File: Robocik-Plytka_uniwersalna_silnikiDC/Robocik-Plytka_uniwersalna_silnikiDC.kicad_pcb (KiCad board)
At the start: 2 copper layers, 60 x 71.1 mm, 67 parts, among them IC1 ACSL-6400-00TE, IC2 L6205D, J1 Conn_01x03, J2 Conn_01x02, J3 Conn_01x04, J4 Conn_01x02, J5 Conn_01x03, J6 Conn_01x02, Q1 BC847, Q2 BC847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

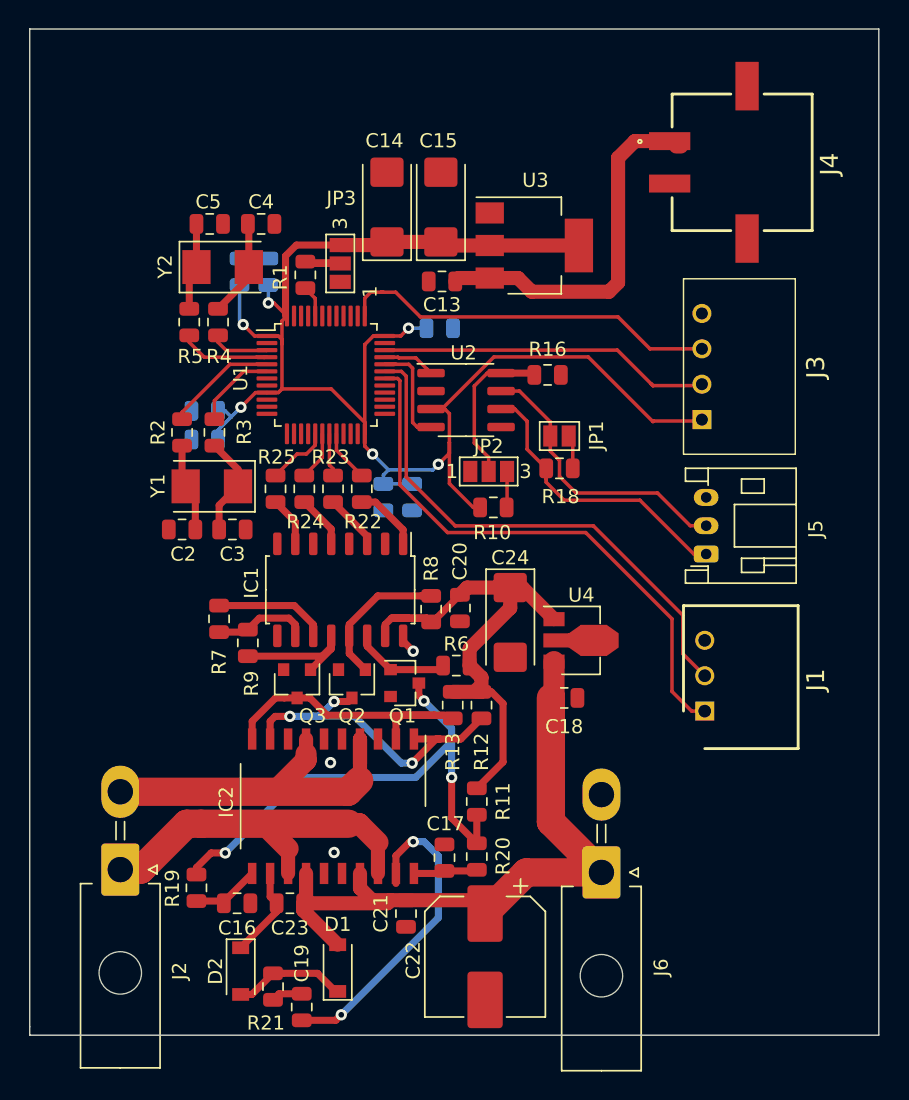
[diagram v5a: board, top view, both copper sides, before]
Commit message: Added 3D model to all connectors, fixed some connections on PCB. Added ground layers for both GNDA and GNDD.
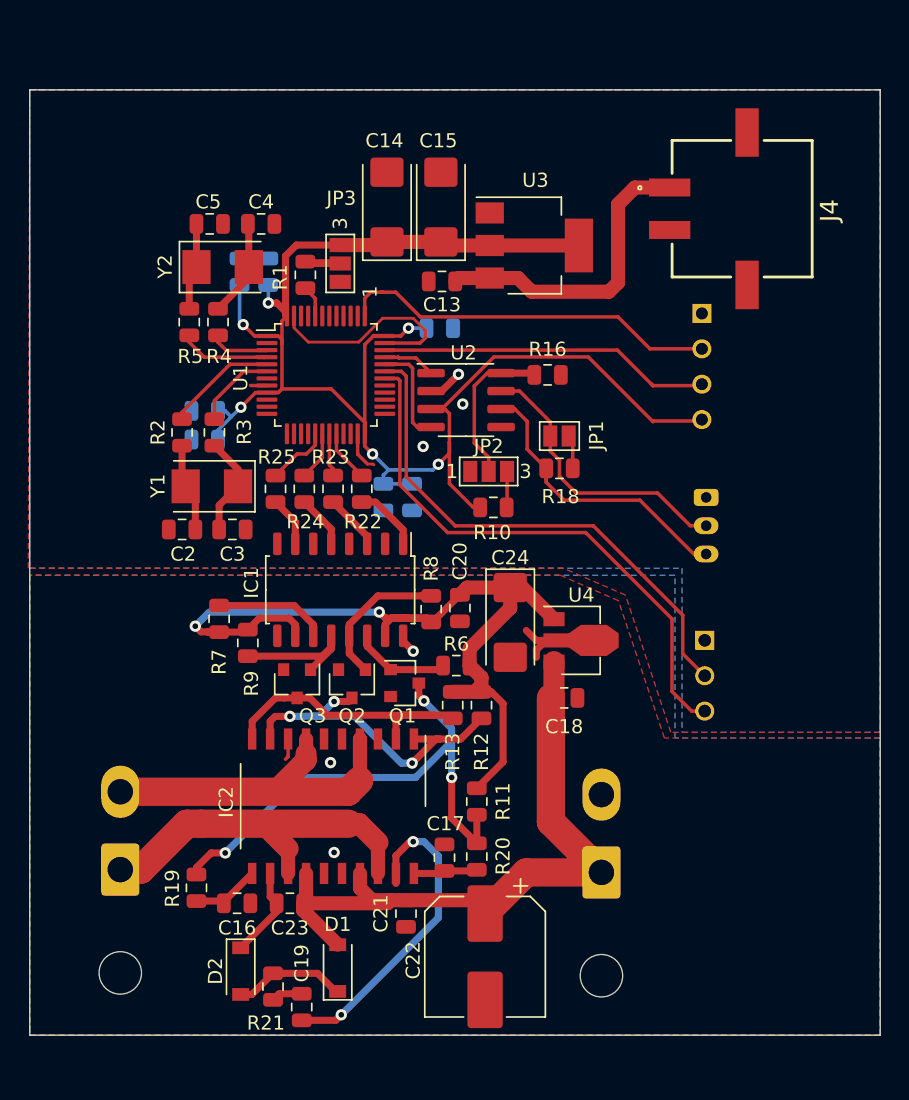
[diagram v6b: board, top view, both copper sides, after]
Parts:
- J1, J2, J3, J5, J6: moved to B.Cu
- moved J3 7.50 mm to (169.5, 85.1), turned to 90 degrees
- moved J1 5.00 mm to (169.7, 108.2), turned to 90 degrees
- moved J5 4.00 mm to (169.8, 98.1), turned to 270 degrees
- moved J4 3.28 mm to (177.3, 77.7)
- turned J2 to 0 degrees
- turned J6 to 0 degrees
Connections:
- J1 pad 1: USART_RX -> GNDD
- J1 pad 3: GNDD -> USART_RX
- J3 pad 1: 3.3VD -> GNDD
- J3 pad 2: JTMS_SWDIO -> JTCK_SWCLK
- J3 pad 3: JTCK_SWCLK -> JTMS_SWDIO
- J3 pad 4: GNDD -> 3.3VD
- J5 pad 1: CAN_L -> GNDD
- J5 pad 3: GNDD -> CAN_L
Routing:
- net GNDD: track 0.00 -> 21.7 mm, vias 0 -> 3
- net 5VPWR: track 48.6 -> 65.0 mm, vias 0 -> 2
- net GNDA: track 1.38 -> 7.47 mm
- net VddD: track 27.2 -> 21.9 mm
- added copper zone on B.Cu, net GNDA
- added copper zone on F.Cu, net GNDA
- added copper zone on B.Cu, net GNDD
- added copper zone on F.Cu, net GNDD
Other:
- board size 60 x 71.1 mm -> 60.1 x 66.8 mm

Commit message: Moved all connectors to the same side of PCB. Redesigned ground planes. Added folder "quick view" which consists of PCB schematic, layout, jpegs of PCB top and bottom side and new added step 3D model.
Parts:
- J1, J2, J3, J5, J6: moved to F.Cu
- moved J3 10.5 mm to (169.5, 95.6), turned to 270 degrees
- moved J1 8.00 mm to (169.7, 116.2), turned to 270 degrees
- moved J5 7.00 mm to (169.8, 105.1), turned to 90 degrees
- turned J2 to 180 degrees
- turned J6 to 180 degrees
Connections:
- J1 pad 1: GNDD -> USART_RX
- J1 pad 3: USART_RX -> GNDD
- J3 pad 1: GNDD -> 3.3VD
- J3 pad 2: JTCK_SWCLK -> JTMS_SWDIO
- J3 pad 3: JTMS_SWDIO -> JTCK_SWCLK
- J3 pad 4: 3.3VD -> GNDD
- J5 pad 1: GNDD -> CAN_L
- J5 pad 3: CAN_L -> GNDD
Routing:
- net ENG1: track 37.5 -> 27.0 mm, vias 0 -> 1
- net (no net): track 0.00 -> 2.40 mm
- net 3.3VD: track 116.7 -> 118.8 mm, vias 6 -> 7
- net VddPWR: track 48.9 -> 47.1 mm, vias 0 -> 1
- net JTMS_SWDIO: track 23.3 -> 25.0 mm, vias 0 -> 1
- net JTCK_SWCLK: track 27.1 -> 28.5 mm, vias 0 -> 1
- net USART_RX: track 39.7 -> 41.0 mm, vias 0 -> 1
- net CAN_L: track 21.7 -> 22.9 mm, vias 0 -> 1
- net CAN_H: track 20.3 -> 21.6 mm, vias 0 -> 1
- net USART_TX: track 37.3 -> 38.3 mm, vias 0 -> 1
- net ENG2: vias 0 -> 1
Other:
- board size 60.1 x 66.8 mm -> 60 x 66.8 mm

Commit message: Added folders for footprints and libraries. Added STM pin configuration to quick view folder
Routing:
- net GNDA: track 7.47 -> 9.87 mm
- net (no net): track 2.40 -> 0.00 mm
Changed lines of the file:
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@@
   (gr_line (start 122.1 69.3) (end 122.1 135.5) (layer Edge.Cuts) (width 0.1))
   (gr_line (start 182.1 69.3) (end 122.1 69.3) (layer Edge.Cuts) (width 0.1))
-  (segment (start 143.93201 107.053222) (end 143.93201 109.16799) (width 0.25) (layer F.Cu) (net 0))
-  (segment (start 144 106.8) (end 144 106.985232) (width 0.25) (layer F.Cu) (net 0))
-  (segment (start 144 106.985232) (end 143.93201 107.053222) (width 0.25) (layer F.Cu) (net 0))
+  (segment (start 143.93201 107.053222) (end 143.93201 109.16799) (width 0.25) (layer F.Cu) (net 76))
+  (segment (start 144 106.8) (end 144 106.985232) (width 0.25) (layer F.Cu) (net 76))
+  (segment (start 144 106.985232) (end 143.93201 107.053222) (width 0.25) (layer F.Cu) (net 76))
   (segment (start 145.176 95.051002) (end 145.866488 95.74149) (width 0.25) (layer F.Cu) (net 1))
   (segment (start 145.176 93.6045) (end 145.176 95.051002) (width 0.25) (layer F.Cu) (net 1))
